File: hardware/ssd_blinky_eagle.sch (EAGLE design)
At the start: 13 parts, among them U1 Tiny85-20-SMT

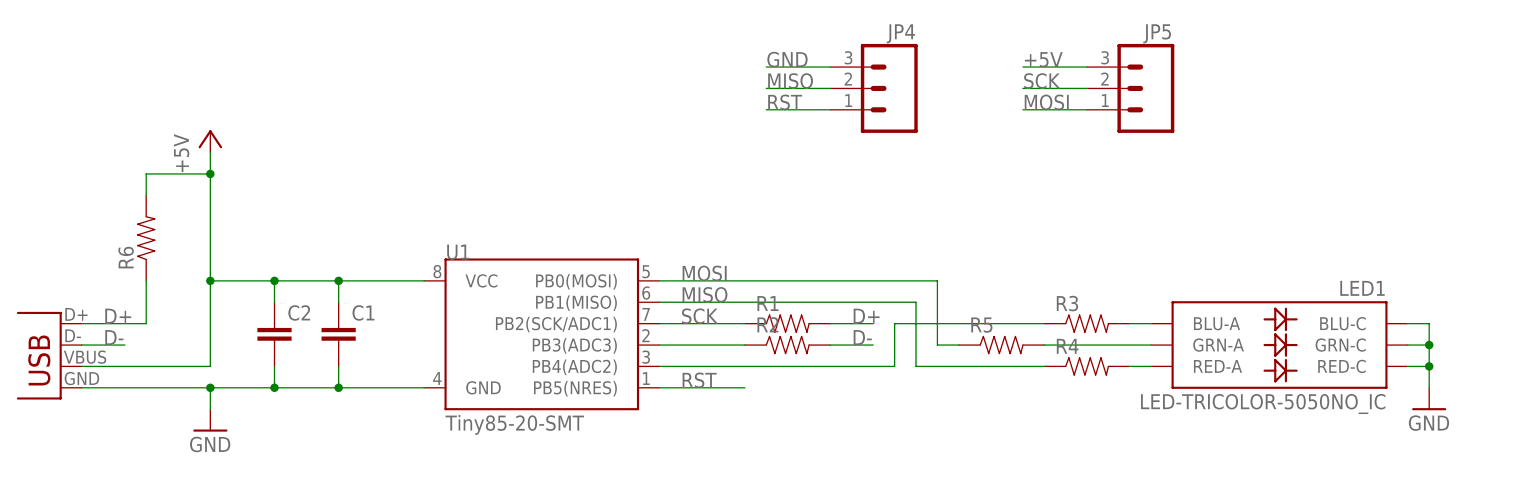
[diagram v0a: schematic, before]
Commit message: complete candidate board layout in eagle
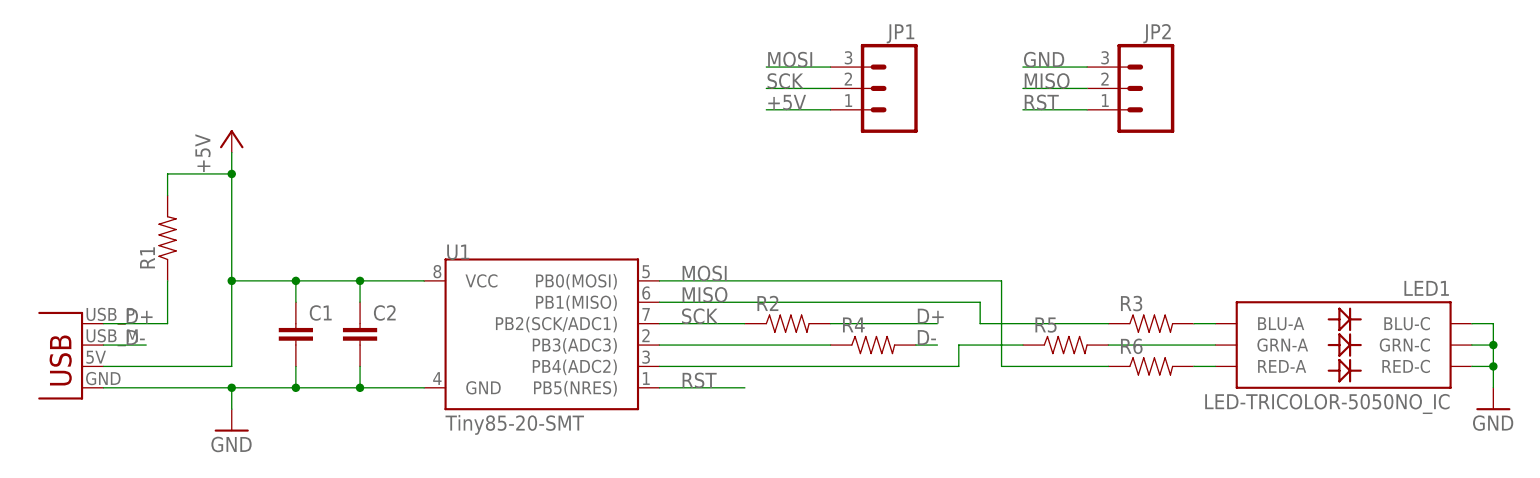
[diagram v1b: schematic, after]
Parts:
- removed JP4: (no value), SparkFun-Connectors:M03SMD_RA_MALE
- added JP3: USBPCB, SparkFun-Connectors:USBPCB
- JP1: value USBSMD -> (none); device SparkFun-Connectors:USBSMD -> SparkFun-Connectors:M03SMD_RA_MALE
- renumbered JP5 to JP2
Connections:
- net +5V: now also JP1.1, JP3.VBUS, R1.2; no longer JP1.VBUS, JP2.3, R6.2
- net D+: now also JP3.D+, R1.1, R2.2; no longer JP1.D+, R1.2, R6.1
- net D-: now also JP3.D-, R4.2; no longer JP1.D-, R2.2
- net GND: now also JP2.3, JP3.GND; no longer JP1.GND, JP4.3
- net MISO: now also JP2.2, R5.1; no longer JP4.2, R3.1
- net MOSI: now also JP1.3, R6.1; no longer JP2.1, R5.1
- net N$1: now also R4.1; no longer R2.1
- net N$2: now also R3.1; no longer R4.1
- net N$4: now also R6.2; no longer R4.2
- net RST: now also JP2.1; no longer JP4.1
- net SCK: now also JP1.2, R2.1; no longer JP2.2, R1.1
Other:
- moved on the sheet: C1, C2, LED1, R1, R2, R3, R4, R5, R6
